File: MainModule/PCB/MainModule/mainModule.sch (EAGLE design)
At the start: 13 parts, among them U1 LM5007MM

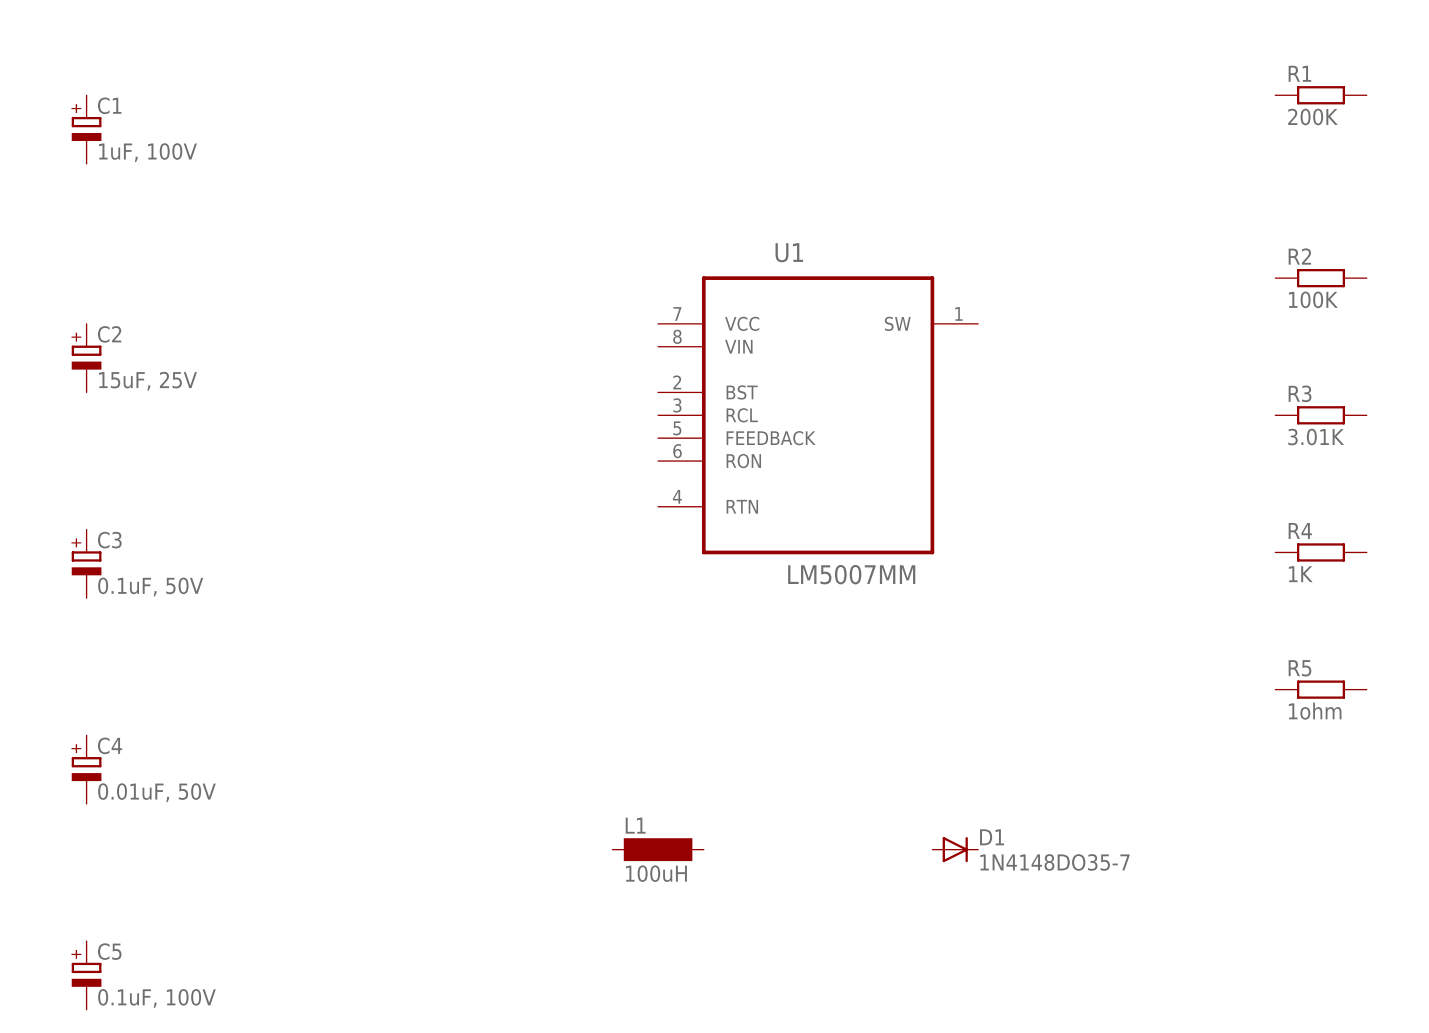
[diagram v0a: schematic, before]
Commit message: Created power supply circuit
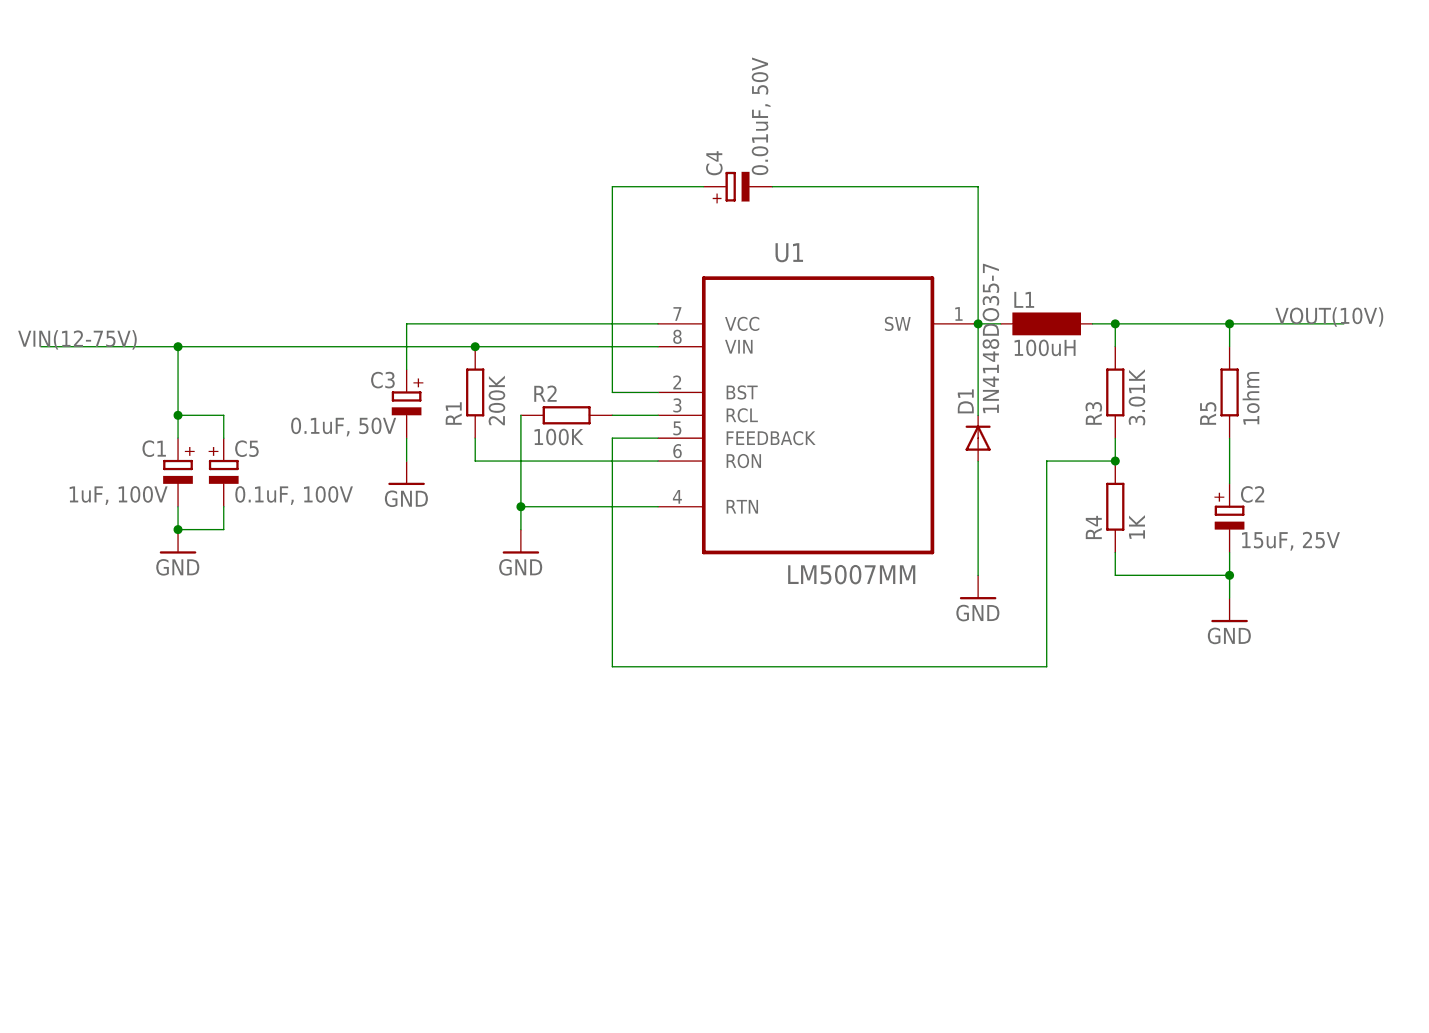
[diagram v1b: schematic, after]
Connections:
- new net GND: C1.-, C2.-, C3.-, C5.-, D1.A, R2.1, R4.1, U1.RTN
- new net N$1: R2.2, U1.RCL
- new net N$3: R1.1, U1.RON
- new net N$5: C4.+, U1.BST
- new net N$6: C4.-, D1.C, L1.1, U1.SW
- new net N$7: C3.+, U1.VCC
- new net N$8: R3.1, R4.2, U1.FEEDBACK
- new net N$9: C2.+, R5.1
- new net VIN(12-75V): C1.+, C5.+, R1.2, U1.VIN
- new net VOUT(10V): L1.2, R3.2, R5.2
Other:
- moved on the sheet: C1, C2, C3, C4, C5, D1, L1, R1, R2, R3, R4, R5

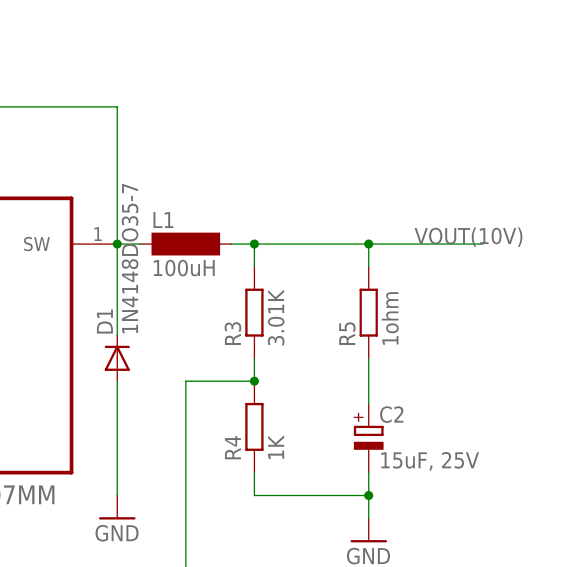
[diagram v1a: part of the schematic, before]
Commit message: changed output voltage form switching power supply
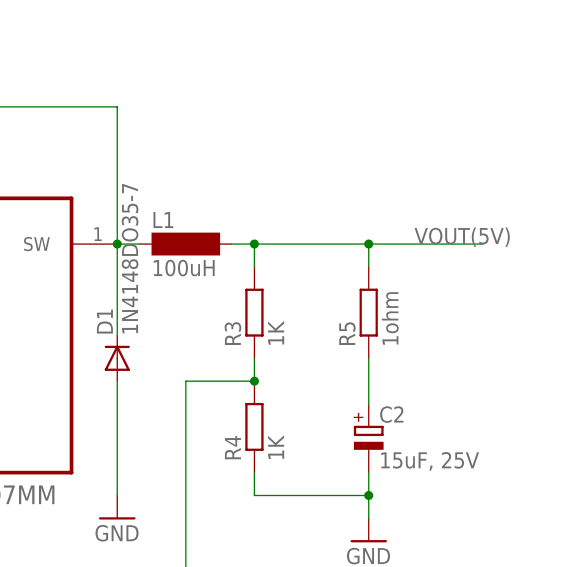
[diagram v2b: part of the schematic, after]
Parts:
- R3: value 3.01K -> 1K
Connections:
- net VOUT(10V) renamed VOUT(5V)
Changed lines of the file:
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@@
 <?xml version="1.0" encoding="utf-8"?>
 <!DOCTYPE eagle SYSTEM "eagle.dtd">
-<eagle version="6.3">
+<eagle version="6.1">
 <drawing>
 <settings>
@@
 <part name="R1" library="rcl" deviceset="R-EU_" device="R2010" value="200K"/>
 <part name="R2" library="rcl" deviceset="R-EU_" device="R2010" value="100K"/>
-<part name="R3" library="rcl" deviceset="R-EU_" device="R2010" value="3.01K"/>
+<part name="R3" library="rcl" deviceset="R-EU_" device="R2010" value="1K"/>
 <part name="R4" library="rcl" deviceset="R-EU_" device="R2010" value="1K"/>
 <part name="R5" library="rcl" deviceset="R-EU_" device="R2010" value="1ohm"/>
@@
 </segment>
 </net>
-<net name="VOUT(10V)" class="0">
+<net name="VOUT(5V)" class="0">
 <segment>
 <pinref part="L1" gate="G$1" pin="2"/>
